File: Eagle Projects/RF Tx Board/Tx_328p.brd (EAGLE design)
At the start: 216.8 x 81.3 mm, 46 parts, among them Q3 16MHz, Q4 16MHz, U1 ATMEGA328P_TQFP, U2 MCP2551

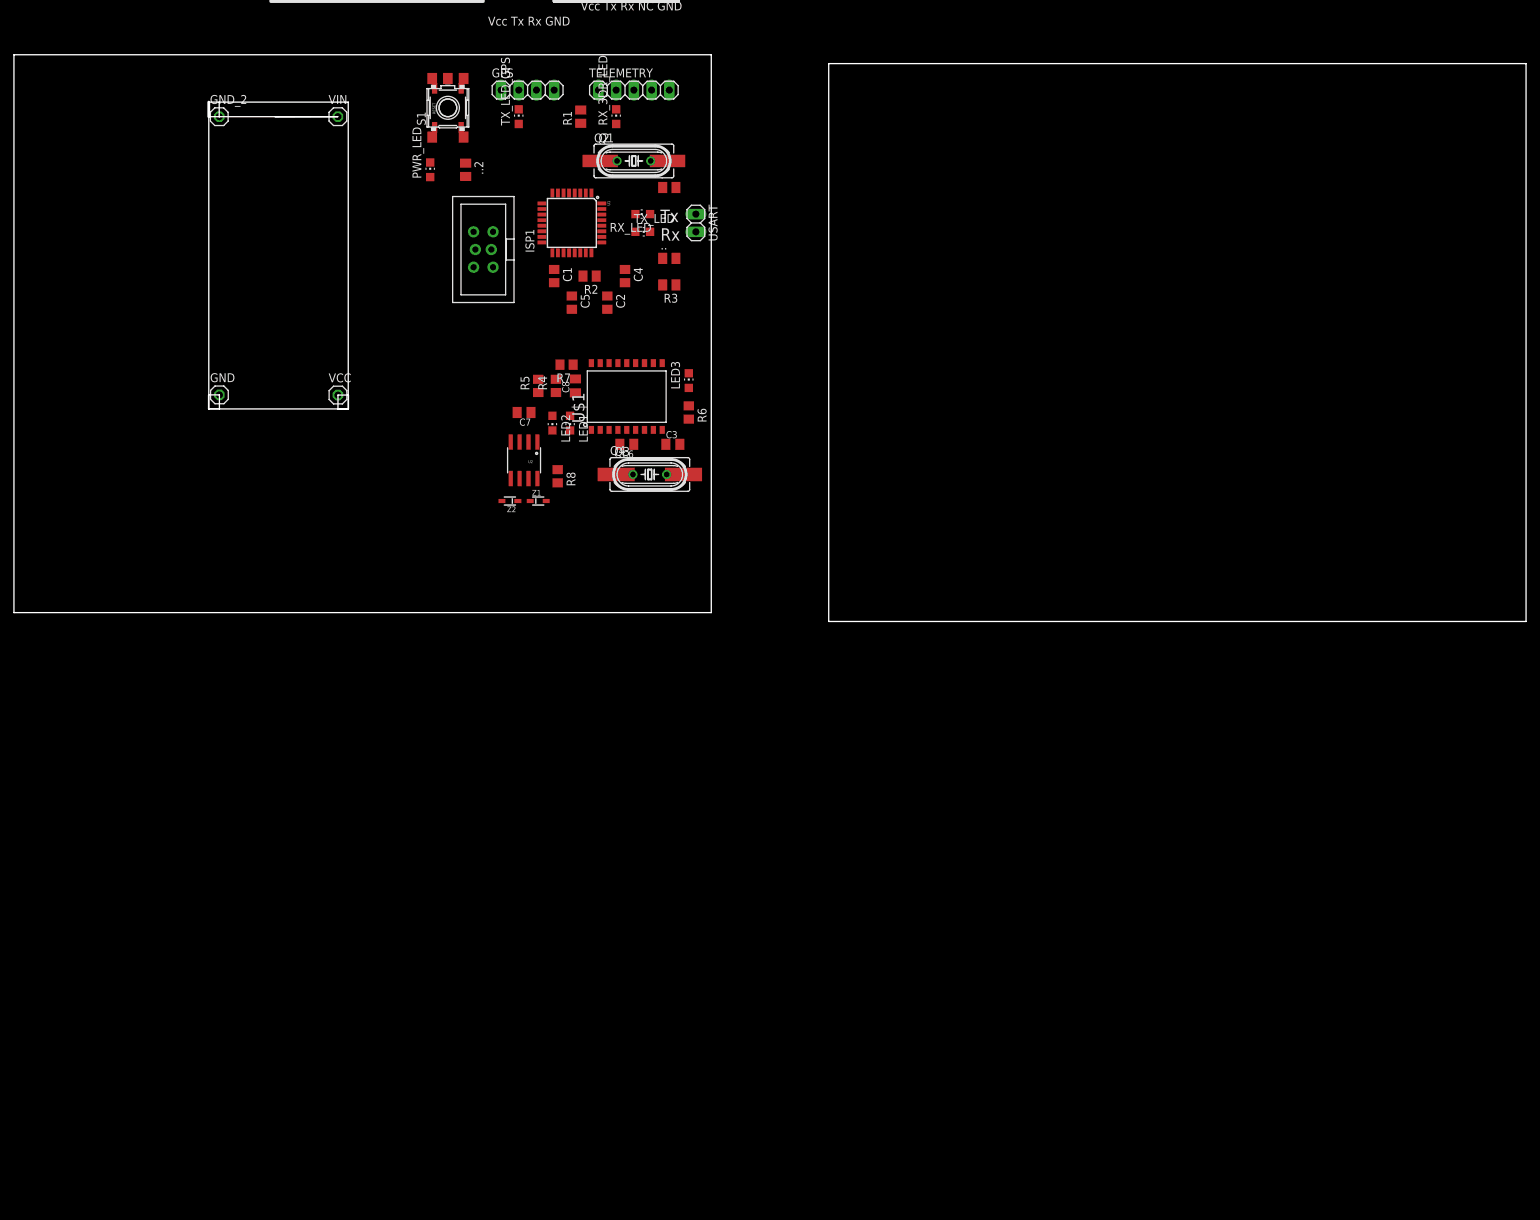
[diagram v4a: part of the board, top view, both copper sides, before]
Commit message: Some routing done on Tx board
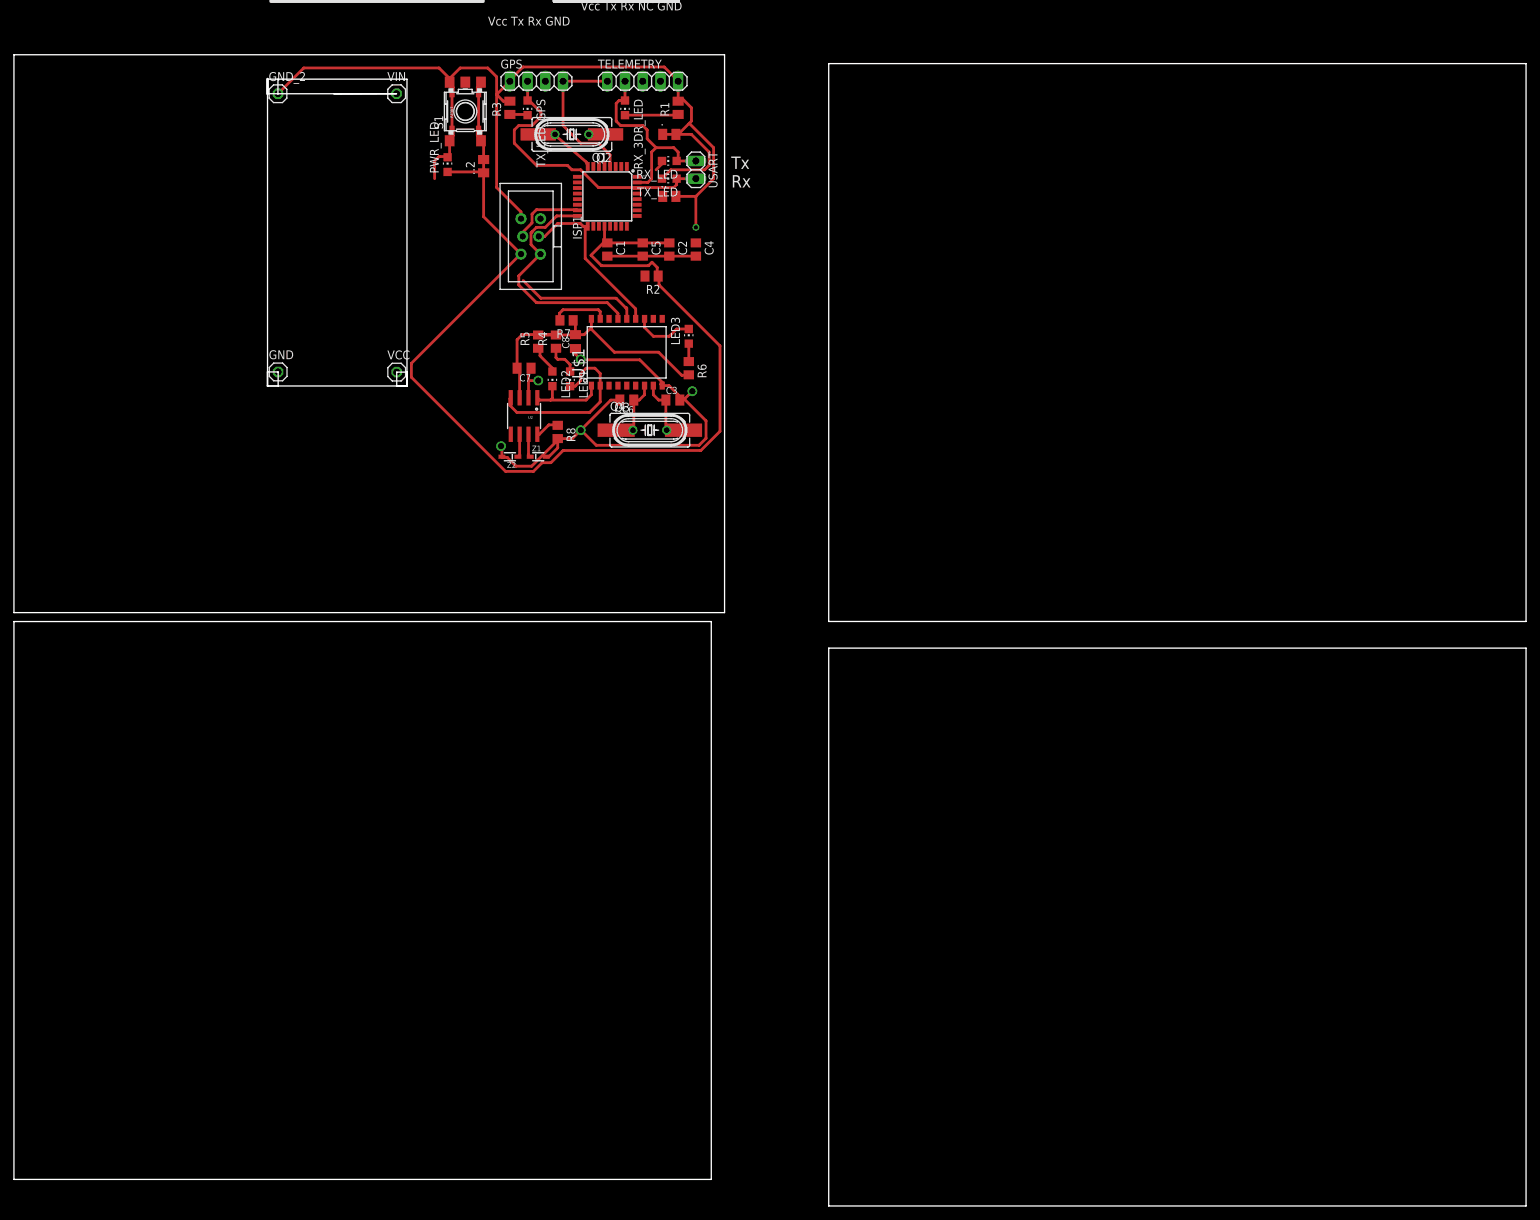
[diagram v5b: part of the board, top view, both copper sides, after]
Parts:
- moved R3 34.2 mm to (71.1, 72.4), turned to 90 degrees
- moved R1 14.0 mm to (95.2, 72.4)
- moved C5 12.7 mm to (90.2, 52.1)
- moved C2 11.7 mm to (94.0, 52.1)
- moved C4 10.9 mm to (97.8, 52.1)
- moved Q1 9.67 mm to (80.0, 68.6), turned to 180 degrees
- moved Q2 9.67 mm to (80.0, 68.6), turned to 180 degrees
- moved GND_2 9.04 mm to (37.9, 74.4)
- moved VIN 9.04 mm to (54.9, 74.4)
- moved VCC 9.04 mm to (54.9, 34.5)
- moved GND 9.04 mm to (37.9, 34.5)
- moved .. 8.89 mm to (94.0, 59.7)
- moved R2 8.89 mm to (91.4, 48.3)
- moved C1 8.52 mm to (85.1, 52.1)
- moved RX_LED 8.52 mm to (94.0, 64.8)
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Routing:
- net GND: track 0.00 -> 230.3 mm, vias 0 -> 6
- net VCC: track 0.00 -> 179.8 mm
- net +5V: track 0.00 -> 44.2 mm
- net RX0: track 0.00 -> 42.3 mm
- net MISO: track 0.00 -> 33.7 mm
- net TX0: track 0.00 -> 29.3 mm
- net MOSI: track 0.00 -> 28.6 mm
- net RXCAN: track 0.00 -> 25.5 mm
- net SCK: track 0.00 -> 24.4 mm
- net N$8: track 0.00 -> 17.2 mm
- net TXCAN: track 0.00 -> 11.6 mm
- net N$13: track 0.00 -> 10.3 mm
- net N$14: track 0.00 -> 10.0 mm
- net N$2: track 0.00 -> 9.46 mm
- net CANINT: track 0.00 -> 8.54 mm
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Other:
- board size 216.8 x 81.3 mm -> 216.8 x 165.1 mm

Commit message: Some Edits to matts board?
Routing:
- net GND: track 230.3 -> 227.6 mm
- net VCC: track 179.8 -> 180.5 mm
- added copper zone on layer 16, net GND
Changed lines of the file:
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@@
 <setting verticaltext="up"/>
 </settings>
-<grid distance="0.025" unitdist="inch" unit="mm" style="lines" multiple="1" display="no" altdistance="0.025" altunitdist="inch" altunit="mm"/>
+<grid distance="0.001" unitdist="inch" unit="inch" style="lines" multiple="1" display="no" altdistance="0.025" altunitdist="inch" altunit="mm"/>
 <layers>
 <layer number="1" name="Top" color="4" fill="1" visible="yes" active="yes"/>
@@
 <layer number="27" name="tValues" color="7" fill="1" visible="yes" active="yes"/>
 <layer number="28" name="bValues" color="7" fill="1" visible="yes" active="yes"/>
-<layer number="29" name="tStop" color="7" fill="3" visible="no" active="yes"/>
-<layer number="30" name="bStop" color="7" fill="6" visible="no" active="yes"/>
-<layer number="31" name="tCream" color="7" fill="4" visible="no" active="yes"/>
-<layer number="32" name="bCream" color="7" fill="5" visible="no" active="yes"/>
-<layer number="33" name="tFinish" color="6" fill="3" visible="no" active="yes"/>
-<layer number="34" name="bFinish" color="6" fill="6" visible="no" active="yes"/>
-<layer number="35" name="tGlue" color="7" fill="4" visible="no" active="yes"/>
-<layer number="36" name="bGlue" color="7" fill="5" visible="no" active="yes"/>
-<layer number="37" name="tTest" color="7" fill="1" visible="no" active="yes"/>
-<layer number="38" name="bTest" color="7" fill="1" visible="no" active="yes"/>
+<layer number="29" name="tStop" color="7" fill="3" visible="yes" active="yes"/>
+<layer number="30" name="bStop" color="7" fill="6" visible="yes" active="yes"/>
+<layer number="31" name="tCream" color="7" fill="4" visible="yes" active="yes"/>
+<layer number="32" name="bCream" color="7" fill="5" visible="yes" active="yes"/>
+<layer number="33" name="tFinish" color="6" fill="3" visible="yes" active="yes"/>
+<layer number="34" name="bFinish" color="6" fill="6" visible="yes" active="yes"/>
+<layer number="35" name="tGlue" color="7" fill="4" visible="yes" active="yes"/>
+<layer number="36" name="bGlue" color="7" fill="5" visible="yes" active="yes"/>
+<layer number="37" name="tTest" color="7" fill="1" visible="yes" active="yes"/>
+<layer number="38" name="bTest" color="7" fill="1" visible="yes" active="yes"/>
 <layer number="39" name="tKeepout" color="4" fill="11" visible="yes" active="yes"/>
 <layer number="40" name="bKeepout" color="1" fill="11" visible="yes" active="yes"/>
@@
 <layer number="42" name="bRestrict" color="1" fill="10" visible="yes" active="yes"/>
 <layer number="43" name="vRestrict" color="2" fill="10" visible="yes" active="yes"/>
-<layer number="44" name="Drills" color="7" fill="1" visible="no" active="yes"/>
-<layer number="45" name="Holes" color="7" fill="1" visible="no" active="yes"/>
-<layer number="46" name="Milling" color="3" fill="1" visible="no" active="yes"/>
-<layer number="47" name="Measures" color="7" fill="1" visible="no" active="yes"/>
+<layer number="44" name="Drills" color="7" fill="1" visible="yes" active="yes"/>
+<layer number="45" name="Holes" color="7" fill="1" visible="yes" active="yes"/>
+<layer number="46" name="Milling" color="3" fill="1" visible="yes" active="yes"/>
+<layer number="47" name="Measures" color="7" fill="1" visible="yes" active="yes"/>
 <layer number="48" name="Document" color="7" fill="1" visible="yes" active="yes"/>
 <layer number="49" name="Reference" color="7" fill="1" visible="yes" active="yes"/>
@@
 <wire x1="216.84" y1="78.73" x2="116.84" y2="78.73" width="0" layer="20"/>
 <wire x1="116.84" y1="78.73" x2="116.84" y2="-1.27" width="0" layer="20"/>
-<wire x1="36.362584375" y1="74.410178125" x2="36.362584375" y2="34.500178125" width="0" layer="20"/>
+<wire x1="36.362584375" y1="74.410178125" x2="36.362584375" y2="34.500178125" width="0" layer="21"/>
 <wire x1="37.862584375" y1="32.500178125" x2="56.362584375" y2="32.500178125" width="0" layer="20"/>
 <wire x1="56.362584375" y1="32.500178125" x2="56.362584375" y2="76.500178125" width="0" layer="20"/>
 <wire x1="56.362584375" y1="76.500178125" x2="36.362584375" y2="76.500178125" width="0" layer="20"/>
-<dimension x1="36.362584375" y1="32.500178125" x2="36.362584375" y2="76.500178125" x3="33.822584375" y3="54.500178125" textsize="3.5" layer="20"/>
-<dimension x1="36.362584375" y1="32.500178125" x2="56.362584375" y2="32.500178125" x3="46.362584375" y3="26.150178125" textsize="3.5" layer="20"/>
+<dimension x1="36.362584375" y1="32.500178125" x2="36.362584375" y2="76.500178125" x3="33.822584375" y3="54.500178125" textsize="3.5" layer="21"/>
+<dimension x1="36.362584375" y1="32.500178125" x2="56.362584375" y2="32.500178125" x3="46.362584375" y3="26.150178125" textsize="3.5" layer="21"/>
 <wire x1="36.362584375" y1="74.410178125" x2="36.362584375" y2="76.500178125" width="0.4064" layer="20"/>
 <wire x1="36.362584375" y1="74.410178125" x2="37.862584375" y2="74.410178125" width="0" layer="20"/>
@@
 <wire x1="37.85845" y1="74.409790625" x2="37.85845" y2="76.506846875" width="0" layer="20"/>
 <wire x1="36.362584375" y1="32.500178125" x2="37.862584375" y2="32.500178125" width="0.254" layer="20"/>
-<wire x1="36.362584375" y1="32.500178125" x2="36.362584375" y2="34.500178125" width="0.254" layer="20"/>
+<wire x1="36.362584375" y1="32.500178125" x2="36.362584375" y2="34.500178125" width="0.254" layer="21"/>
 <wire x1="36.360096875" y1="34.512684375" x2="37.887390625" y2="34.512684375" width="0" layer="20"/>
 <wire x1="37.887390625" y1="34.512684375" x2="37.887390625" y2="32.493346875" width="0" layer="20"/>
@@
 <wire x1="70.75" y1="22.25" x2="70" y2="22.25" width="0.4064" layer="1"/>
 <wire x1="72" y1="21" x2="70.75" y2="22.25" width="0.4064" layer="1"/>
-<wire x1="74.25" y1="21" x2="72" y2="21" width="0.4064" layer="1"/>
-<wire x1="78" y1="24.75" x2="74.25" y2="21" width="0.4064" layer="1"/>
+<wire x1="74.975" y1="21" x2="72" y2="21" width="0.4064" layer="1"/>
 <wire x1="70" y1="22.25" x2="69.977" y2="22.352" width="0.4064" layer="1"/>
 <wire x1="78" y1="24.75" x2="77.978" y2="24.958" width="0.4064" layer="1"/>
@@
 <wire x1="71.12" y1="73.34" x2="70.17" y2="73.34" width="0.4064" layer="1"/>
 <wire x1="70.17" y1="73.34" x2="69.215" y2="74.295" width="0.4064" layer="1"/>
+<wire x1="74.975" y1="21" x2="76.327" y2="22.352" width="0.4064" layer="1"/>
+<polygon width="0.6096" layer="16" isolate="0.4064">
+<vertex x="0" y="0"/>
+<vertex x="101.9048" y="0"/>
+<vertex x="101.9048" y="80.01"/>
+<vertex x="0" y="80.01"/>
+</polygon>
 <wire x1="97.79" y1="55.245" x2="97.79" y2="51.12" width="0" layer="19" extent="1-1"/>
-<wire x1="80.518" y1="37.862" x2="85.09" y2="51.12" width="0" layer="19" extent="1-1"/>
-<wire x1="75.184" y1="33.274" x2="80.518" y2="37.084" width="0" layer="19" extent="1-1"/>
-<wire x1="37.886703125" y1="34.51426875" x2="69.85" y2="23.876" width="0" layer="19" extent="1-1"/>
 </signal>
 <signal name="N$3">
@@
 <wire x1="101.25" y1="38.25" x2="92.5" y2="47" width="0.4064" layer="1"/>
 <wire x1="101.25" y1="26" x2="101.25" y2="38.25" width="0.4064" layer="1"/>
-<wire x1="98.5" y1="23.25" x2="101.25" y2="26" width="0.4064" layer="1"/>
-<wire x1="78.75" y1="23.25" x2="98.5" y2="23.25" width="0.4064" layer="1"/>
-<wire x1="77" y1="21.5" x2="78.75" y2="23.25" width="0.4064" layer="1"/>
-<wire x1="75.75" y1="21.5" x2="77" y2="21.5" width="0.4064" layer="1"/>
-<wire x1="74.5" y1="20.25" x2="75.75" y2="21.5" width="0.4064" layer="1"/>
-<wire x1="70.5" y1="20.25" x2="74.5" y2="20.25" width="0.4064" layer="1"/>
-<wire x1="57" y1="33.75" x2="70.5" y2="20.25" width="0.4064" layer="1"/>
+<wire x1="57" y1="33.75" x2="70.811" y2="19.939" width="0.4064" layer="1"/>
 <wire x1="57" y1="35.75" x2="57" y2="33.75" width="0.4064" layer="1"/>
 <wire x1="72.5" y1="51.25" x2="57" y2="35.75" width="0.4064" layer="1"/>
 <wire x1="92.5" y1="48.25" x2="92.39" y2="48.26" width="0.4064" layer="1"/>
 <wire x1="72.5" y1="51.25" x2="72.713665625" y2="51.41195" width="0.4064" layer="1"/>
+<wire x1="101.25" y1="26" x2="101.2444" y2="25.9944" width="0.4064" layer="1"/>
+<wire x1="101.2444" y1="25.9944" x2="101.2444" y2="25.2476" width="0.4064" layer="1"/>
+<wire x1="101.2444" y1="25.2476" x2="98.8314" y2="22.8346" width="0.4064" layer="1"/>
+<wire x1="98.8314" y1="22.8346" x2="79.1718" y2="22.8346" width="0.4064" layer="1"/>
+<wire x1="79.1718" y1="22.8346" x2="76.2762" y2="19.939" width="0.4064" layer="1"/>
+<wire x1="76.2762" y1="19.939" x2="70.811" y2="19.939" width="0.4064" layer="1"/>
 <wire x1="84.69" y1="55.3974" x2="85.49" y2="63.9826" width="0" layer="19" extent="1-1"/>
 <wire x1="83.09" y1="55.3974" x2="84.69" y2="55.3974" width="0" layer="19" extent="1-1"/>
